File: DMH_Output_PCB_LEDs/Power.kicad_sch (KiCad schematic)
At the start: 79 parts, among them J0 Conn_01x01, J10 Conn_01x06, J100 IDC_02x05, J23 Conn_01x06, U1 TL072, U10 NE5532, U11 TL074, U12 NE5532, U13 NE5532, U14 NE5532, U15 NE5532, U16 NE5532, U17 NE5532, U18 NE5532, U19 NE5532, U2 LM339, U20 TL072, U21 LM4040LP-10, U24 LM339, U25 LM339, U3 LM339, U4 LM339, U5 LM339, U6 LM339, U7 TL072, U8 TL074, U9 NE5532

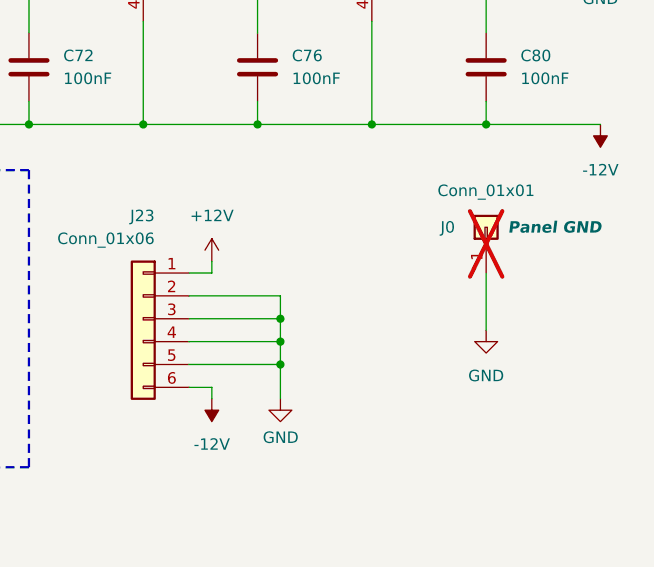
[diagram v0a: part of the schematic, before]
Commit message: Regenerated LEDs baffle Gerbers
Added second GND plated hole to avoid issues with the probe test at JLC
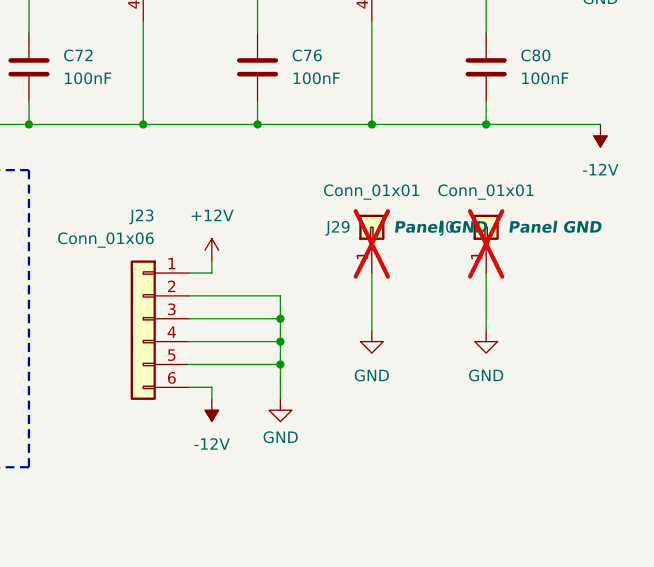
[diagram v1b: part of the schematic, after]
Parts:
- added J29: Conn_01x01, Connector_PinHeader_2.54mm:PinHeader_1x01_P2.54mm_Vertical, symbol Connector_Generic:Conn_01x01
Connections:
- net GND: now also J29.1 (Pin_1)
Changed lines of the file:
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@@
+	(wire
+		(pts
+			(xy 254 143.51) (xy 254 149.86)
+		)
+		(stroke
+			(width 0)
+			(type default)
+		)
+	)
 	(wire
 		(pts
@@
 				(path "/58f4306d-5387-4983-bb08-41a2313fd315/0cdf34b2-39cd-4d9e-981a-97cd34791509"
 					(reference "C76")
+					(unit 1)
+				)
+			)
+		)
+	)
+	(symbol
+		(lib_id "power:GND")
+		(at 254 149.86 0)
+		(unit 1)
+		(exclude_from_sim no)
+		(in_bom yes)
+		(on_board yes)
+		(dnp no)
+		(fields_autoplaced yes)
+		(property "Reference" "#PWR094"
+			(at 254 156.21 0)
+			(effects
+				(font
+					(size 1.27 1.27)
+				)
+				(hide yes)
+			)
+		)
+		(property "Value" "GND"
+			(at 254 154.94 0)
+			(effects
+				(font
+					(size 1.27 1.27)
+				)
+			)
+		)
+		(property "Footprint" ""
+			(at 254 149.86 0)
+			(effects
+				(font
+					(size 1.27 1.27)
+				)
+				(hide yes)
+			)
+		)
+		(property "Datasheet" ""
+			(at 254 149.86 0)
+			(effects
+				(font
+					(size 1.27 1.27)
+				)
+				(hide yes)
+			)
+		)
+		(property "Description" "Power symbol creates a global label with name \"GND\" , ground"
+			(at 254 149.86 0)
+			(effects
+				(font
+					(size 1.27 1.27)
+				)
+				(hide yes)
+			)
+		)
+		(pin "1"
+		)
+		(instances
+			(project "DMH_Output_PCB_LEDs"
+				(path "/58f4306d-5387-4983-bb08-41a2313fd315/0cdf34b2-39cd-4d9e-981a-97cd34791509"
+					(reference "#PWR094")
 					(unit 1)
 				)
@@
 					(unit 1)
 				)
+			)
+		)
+	)
+	(symbol
+		(lib_id "Connector_Generic:Conn_01x01")
+		(at 254 138.43 90)
+		(unit 1)
+		(exclude_from_sim no)
+		(in_bom no)
+		(on_board yes)
+		(dnp yes)
+		(property "Reference" "J29"
+			(at 248.92 138.43 90)
+			(effects
+				(font
+					(size 1.27 1.27)
+				)
+				(justify right)
+			)
+		)
+		(property "Value" "Conn_01x01"
+			(at 254 134.366 90)
+			(effects
+				(font
+					(size 1.27 1.27)
+				)
+			)
+		)
+		(property "Footprint" "Connector_PinHeader_2.54mm:PinHeader_1x01_P2.54mm_Vertical"
+			(at 254 138.43 0)
+			(effects
+				(font
+					(size 1.27 1.27)
+				)
+				(hide yes)
+			)
+		)
+		(property "Datasheet" "~"
+			(at 254 138.43 0)
+			(effects
+				(font
+					(size 1.27 1.27)
+				)
+				(hide yes)
+			)
+		)
+		(property "Description" "Generic connector, single row, 01x01, script generated (kicad-library-utils/schlib/autogen/connector/)"
+			(at 254 138.43 0)
+			(effects
+				(font
+					(size 1.27 1.27)
+				)
+				(hide yes)
+			)
+		)
+		(property "Function" "Panel GND"
+			(at 261.62 138.43 90)
+			(effects
+				(font
+					(size 1.27 1.27)
+					(thickness 0.254)
+					(bold yes)
+					(italic yes)
+				)
+			)
+		)
+		(pin "1"
+		)
+		(instances
+			(project "DMH_Output_PCB_LEDs"
+				(path "/58f4306d-5387-4983-bb08-41a2313fd315/0cdf34b2-39cd-4d9e-981a-97cd34791509"
+					(reference "J29")
+					(unit 1)
+				)

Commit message: Re-exported all Gerbers
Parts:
- removed H23: MountingHole, MountingHole:MountingHole_2.2mm_M2, symbol Mechanical:MountingHole
- H21, H22: footprint MountingHole:MountingHole_2.2mm_M2 -> MountingHole:MountingHole_2.7mm_M2.5_ISO14580
